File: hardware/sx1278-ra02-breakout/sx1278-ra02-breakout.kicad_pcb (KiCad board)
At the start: 2 copper layers, 17.5 x 22.5 mm, 2 parts, among them J1 SX1278_Ra-02_breakout, U1 Ra-02

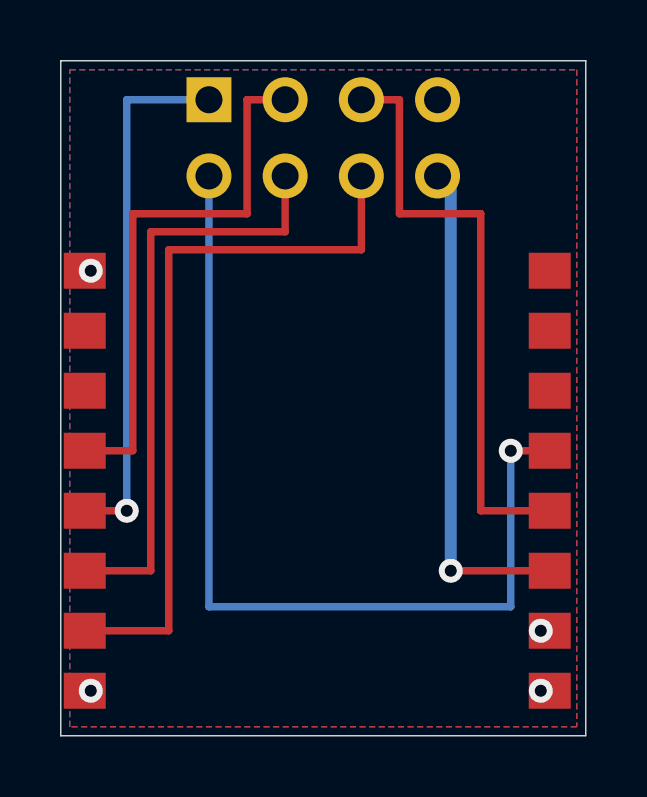
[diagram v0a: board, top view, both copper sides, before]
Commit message: Merge the two socket adapters into esp32c3-radio-adapter; two-sided pin silk on the replicas
* esp32c3-radio-adapter replaces esp32c3-cc1101-adapter and
  esp32c3-ra02-adapter: the E07-M1101D and Ra-02 breakout headers differ
  only at outer column 3 (GDO0 / RST) and inner column 1 (GDO2 / DIO0),
  wired to GPIO10 and GPIO3, so one socket takes either board.  Nets are
  named GDO0_RST, GDO2_DIO0 and CSN_NSS; the silk carries the E07 names
  with the Ra-02 names in parentheses, plus both boards' fab outlines.
* Ra-02 breakout replica: header and module pin numbers on the back silk;
  header pin names beside each column on both sides.
* E07-M1101D replica: pin names beside each column on both sides; the
  markers, box and legend are mirrored onto the back.
* Pinout diagrams combined into docs/images/pinout-radio-boards.svg.
* README, export defaults and generator lists updated.

Co-Authored-By: Claude Fable 5.1 <noreply@anthropic.com>
Claude-Session: https://claude.ai/code/session_01JoGdh4Cg3VtTTDZi4gQuiN
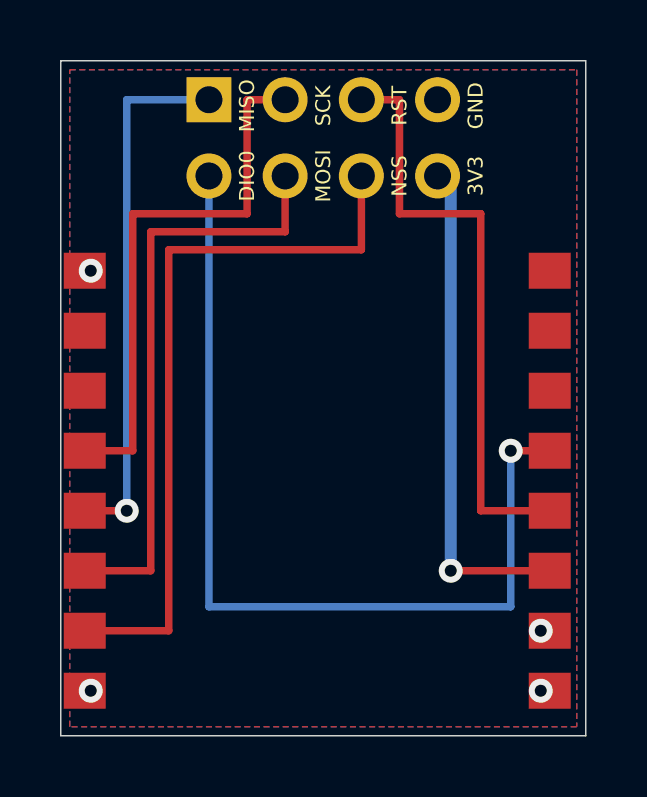
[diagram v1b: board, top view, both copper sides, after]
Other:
- board text added: "1"
- board text added: "10"
- board text added: "11"
- board text added: "12"
- board text added: "13"
- board text added: "14"
- board text added: "15"
- board text added: "16"
- board text added: "2"
- board text added: "3"
- board text added: "4"
- board text added: "5"
- board text added: "6"
- board text added: "7"
- board text added: "8"
- board text added: "9"
